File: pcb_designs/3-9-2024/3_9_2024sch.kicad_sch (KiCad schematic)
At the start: 19 parts, among them J1 Conn_01x05_Socket, J3 Conn_01x17_Pin, J4 Conn_01x17_Pin, J5 Conn_01x05_Socket, SW1 A_Button, SW10 Left_Button, SW11 Select_Button, SW12 Start_Button, SW13 Up_Button, SW14 Down_Button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

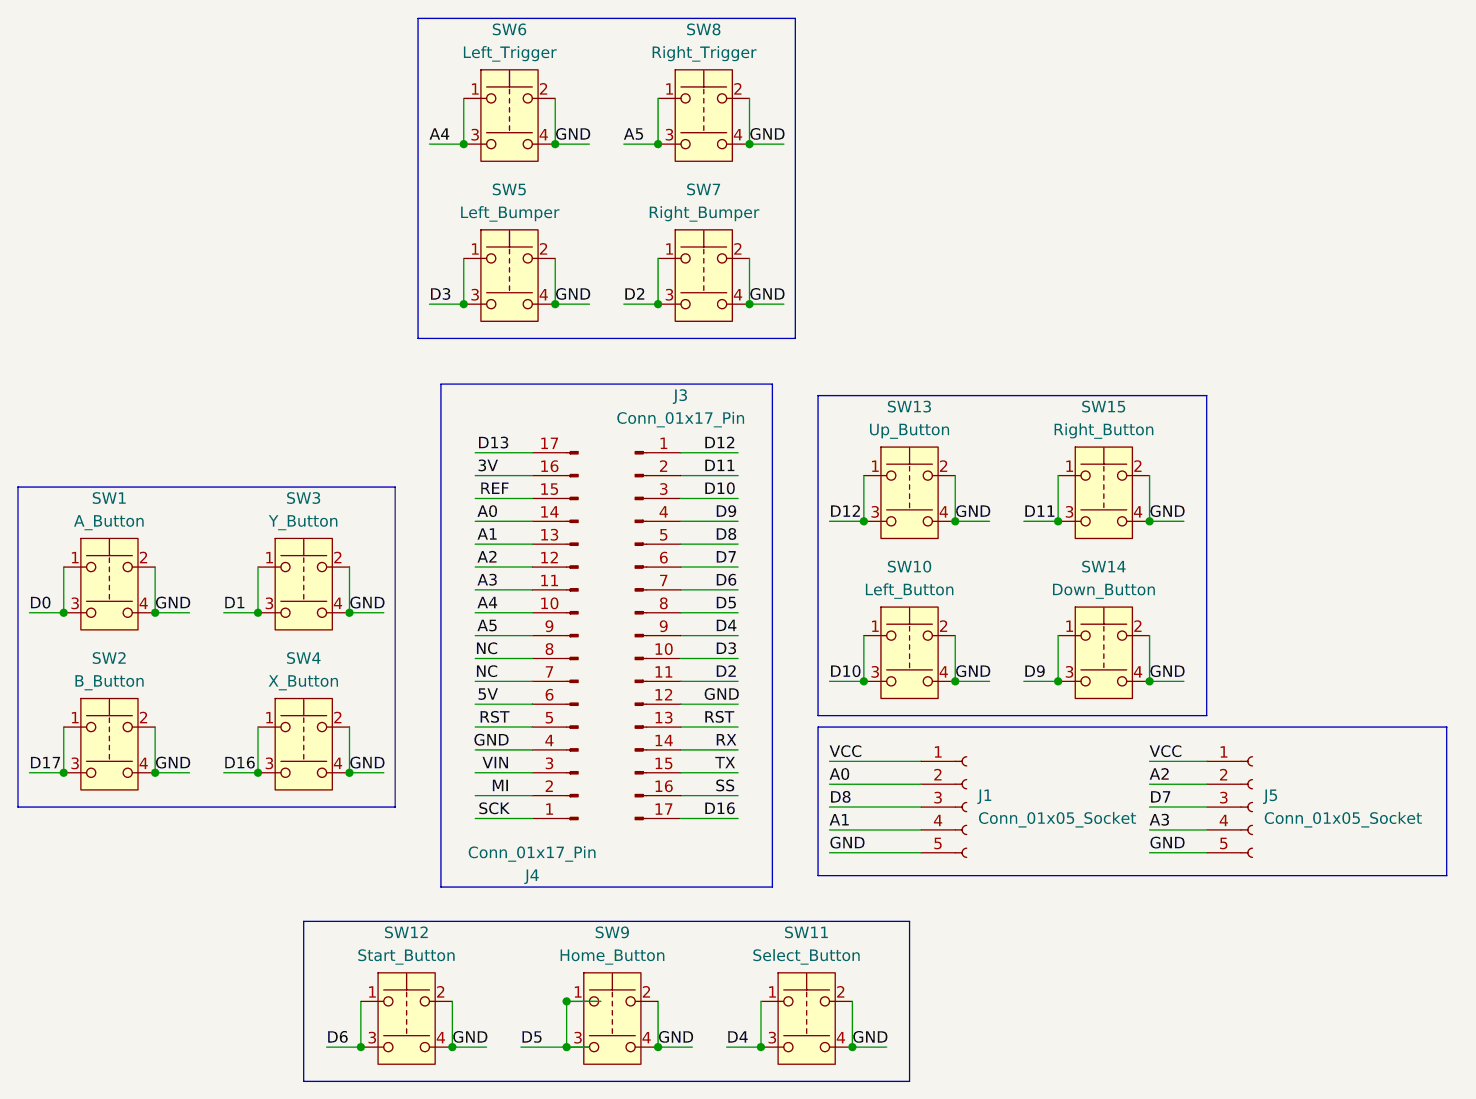
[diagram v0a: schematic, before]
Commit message: :construction: finish draft 1 of wiring
- changed symbols to two-prong buttons

- finished initial draft of wiring
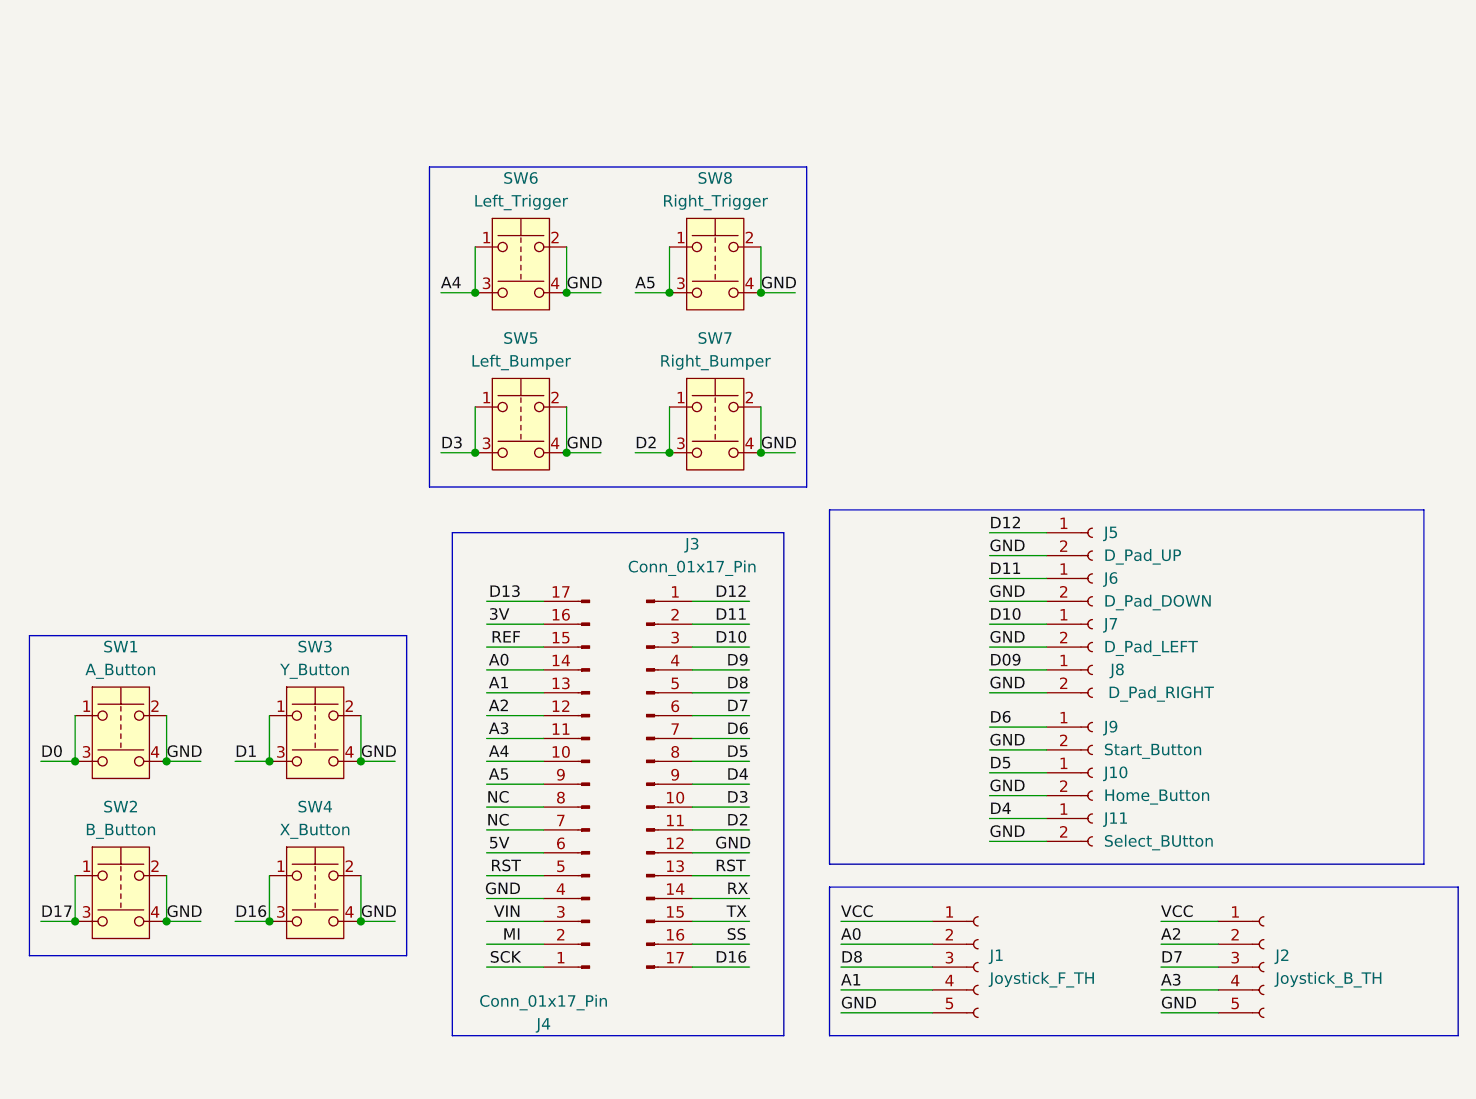
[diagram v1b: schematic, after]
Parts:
- removed SW10: Left_Button, Button_Switch_THT:Push_E-Switch_KS01Q01, symbol Switch:SW_Push_Dual
- removed SW11: Select_Button, Button_Switch_THT:Push_E-Switch_KS01Q01, symbol Switch:SW_Push_Dual
- removed SW12: Start_Button, Button_Switch_THT:Push_E-Switch_KS01Q01, symbol Switch:SW_Push_Dual
- removed SW13: Up_Button, Button_Switch_THT:Push_E-Switch_KS01Q01, symbol Switch:SW_Push_Dual
- removed SW14: Down_Button, Button_Switch_THT:Push_E-Switch_KS01Q01, symbol Switch:SW_Push_Dual
- removed SW15: Right_Button, Button_Switch_THT:Push_E-Switch_KS01Q01, symbol Switch:SW_Push_Dual
- removed SW9: Home_Button, Button_Switch_THT:Push_E-Switch_KS01Q01, symbol Switch:SW_Push_Dual
- added J10: Home_Button, Connector_Wire:SolderWire-0.1sqmm_1x02_P3.6mm_D0.4mm_OD1mm, symbol Connector:Conn_01x02_Socket
- added J11: Select_BUtton, Connector_Wire:SolderWire-0.1sqmm_1x02_P3.6mm_D0.4mm_OD1mm, symbol Connector:Conn_01x02_Socket
- added J5: D_Pad_UP, Connector_Wire:SolderWire-0.1sqmm_1x02_P3.6mm_D0.4mm_OD1mm, symbol Connector:Conn_01x02_Socket
- added J6: D_Pad_DOWN, Connector_Wire:SolderWire-0.1sqmm_1x02_P3.6mm_D0.4mm_OD1mm, symbol Connector:Conn_01x02_Socket
- added J7: D_Pad_LEFT, Connector_Wire:SolderWire-0.1sqmm_1x02_P3.6mm_D0.4mm_OD1mm, symbol Connector:Conn_01x02_Socket
- added J8: D_Pad_RIGHT, Connector_Wire:SolderWire-0.1sqmm_1x02_P3.6mm_D0.4mm_OD1mm, symbol Connector:Conn_01x02_Socket
- added J9: Start_Button, Connector_Wire:SolderWire-0.1sqmm_1x02_P3.6mm_D0.4mm_OD1mm, symbol Connector:Conn_01x02_Socket
- J1: value Conn_01x05_Socket -> Joystick_F_TH; footprint (none) -> Connector_Wire:SolderWire-0.1sqmm_1x05_P3.6mm_D0.4mm_OD1mm
- J2: renamed from J5; value Conn_01x05_Socket -> Joystick_B_TH; footprint (none) -> Connector_Wire:SolderWire-0.1sqmm_1x05_P3.6mm_D0.4mm_OD1mm
- SW1, SW2, SW3, SW4, SW5, SW6, SW7, SW8: footprint Button_Switch_THT:Push_E-Switch_KS01Q01 -> Downloads:D6R90_CNK
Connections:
- net D10: now also J7.1 (Pin_1)
- net D11: now also J6.1 (Pin_1)
- net D12: now also J5.1 (Pin_1)
- net D4: now also J11.1 (Pin_1)
- net D5: now also J10.1 (Pin_1)
- net D6: now also J9.1 (Pin_1)
- net GND: now also J10.2 (Pin_2), J11.2 (Pin_2), J5.2 (Pin_2), J6.2 (Pin_2), J7.2 (Pin_2), J8.2 (Pin_2), J9.2 (Pin_2)
- new net D09: J8.1 (Pin_1)
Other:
- moved on the sheet: J1, J2, J3, J4, SW1, SW2, SW3, SW4, SW5, SW6, SW7, SW8
